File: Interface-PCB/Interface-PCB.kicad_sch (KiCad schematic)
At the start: 16 parts, among them J1 BARREL_JACK_PAD, J2 BARREL_JACK_PAD, J3 GPIO_DEBUG_HEADER, J4 RASPBERRYPI_GPIO_CONN_HEADER, M1 PERISTALTIC_PUMP, M2 PERISTALTIC_PUMP, M3 PERISTALTIC_PUMP, U1 TB6612FNG_BREAKOUT, U2 TB6612FNG_BREAKOUT

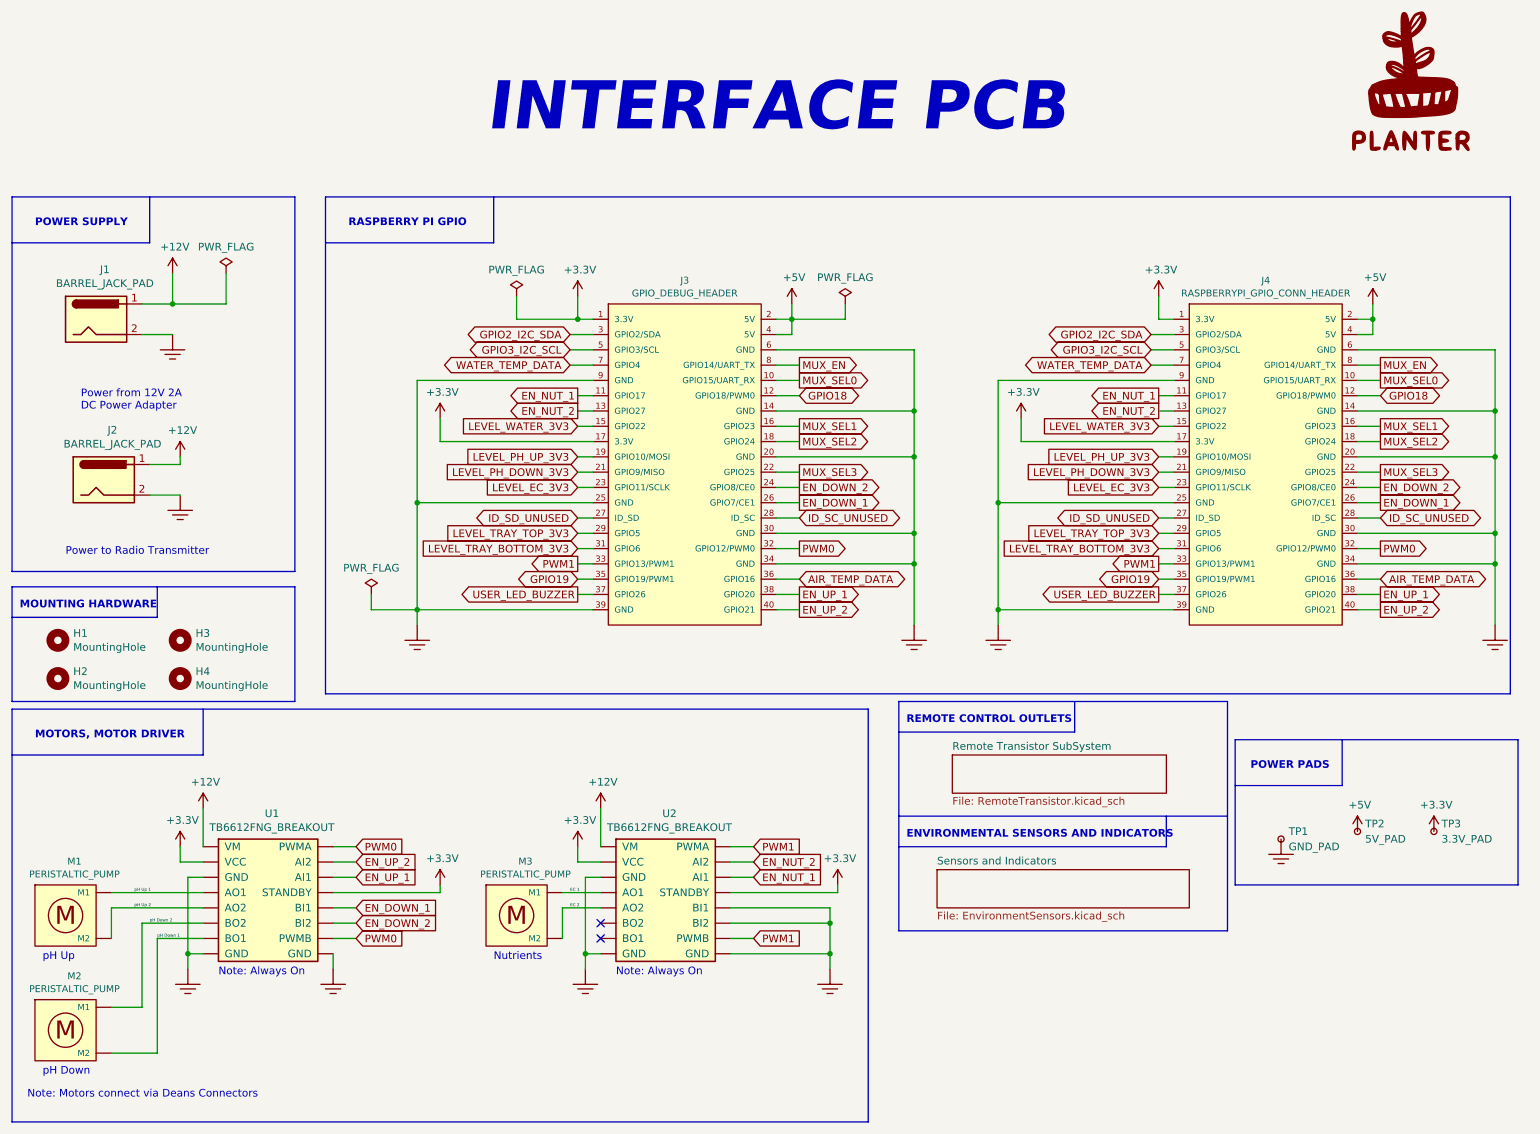
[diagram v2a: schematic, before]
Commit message: Align DIP-socket resistors with 2.54mm pin spacing
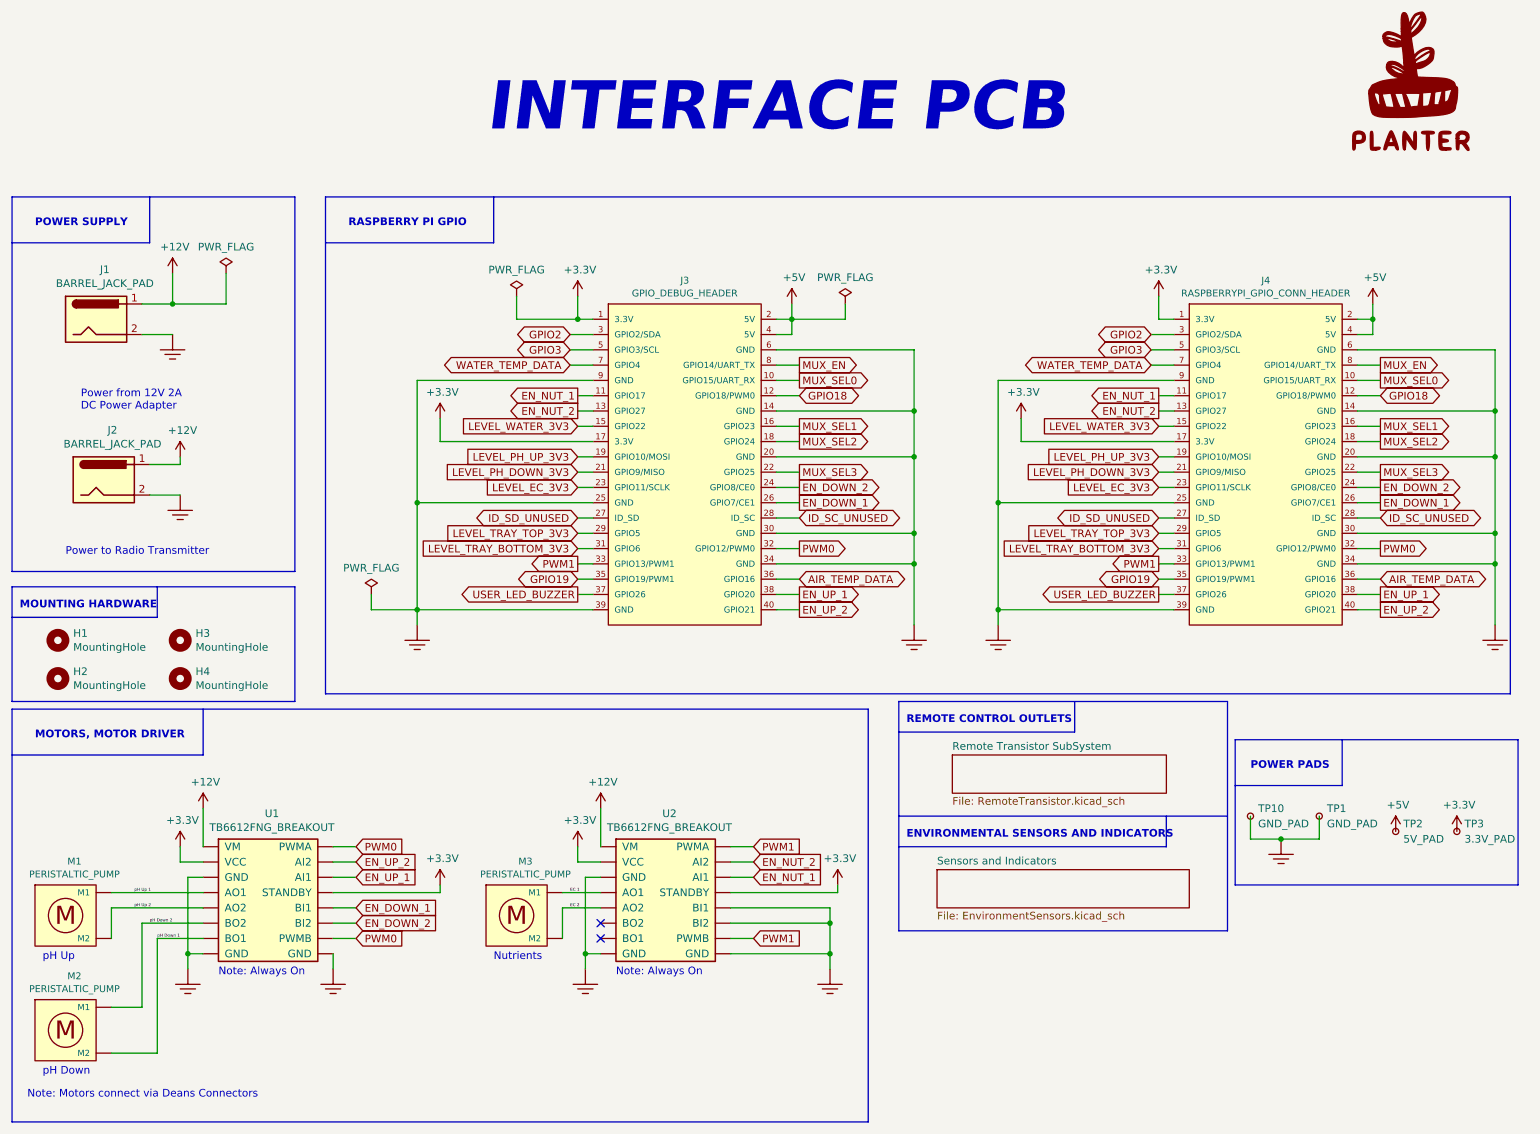
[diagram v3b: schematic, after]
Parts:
- added TP10: GND_PAD, AA_Custom_Components:TestPoint_Pad_5.0x5.0mm, symbol Connector:TestPoint_Small
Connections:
- net GND: now also TP10.1
- net GPIO2_I2C_SDA renamed GPIO2
- net GPIO3_I2C_SCL renamed GPIO3
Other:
- moved on the sheet: TP1, TP2, TP3
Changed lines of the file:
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@@
   (junction (at 151.13 168.91) (diameter 0) (color 0 0 0 0)
+  )
+  (junction (at 226.06 154.94) (diameter 0) (color 0 0 0 0)
   )
   (junction (at 261.62 109.22) (diameter 0) (color 0 0 0 0)
@@
     (stroke (width 0) (type default) (color 0 0 0 0))
   )
+  (wire (pts (xy 232.41 151.13) (xy 232.41 154.94))
+    (stroke (width 0) (type default) (color 0 0 0 0))
+  )
   (polyline (pts (xy 264.16 130.81) (xy 67.31 130.81))
     (stroke (width 0) (type default) (color 0 0 0 0))
@@
     (stroke (width 0) (type default) (color 0 0 0 0))
   )
+  (wire (pts (xy 232.41 154.94) (xy 226.06 154.94))
+    (stroke (width 0) (type default) (color 0 0 0 0))
+  )
   (wire (pts (xy 238.76 96.52) (xy 242.57 96.52))
     (stroke (width 0) (type default) (color 0 0 0 0))
@@
     (stroke (width 0) (type default) (color 0 0 0 0))
   )
+  (wire (pts (xy 220.98 154.94) (xy 226.06 154.94))
+    (stroke (width 0) (type default) (color 0 0 0 0))
+  )
   (wire (pts (xy 72.39 171.45) (xy 68.58 171.45))
     (stroke (width 0) (type default) (color 0 0 0 0))
@@
   )
   (wire (pts (xy 109.22 86.36) (xy 111.76 86.36))
+    (stroke (width 0) (type default) (color 0 0 0 0))
+  )
+  (wire (pts (xy 220.98 151.13) (xy 220.98 154.94))
     (stroke (width 0) (type default) (color 0 0 0 0))
   )
@@
     )
   )
-  (global_label "GPIO3_I2C_SCL" (shape bidirectional) (at 107.95 73.66 180) (fields_autoplaced)
-    (effects (font (size 1.27 1.27)) (justify right))
-    (property "Intersheet References" "${INTERSHEET_REFS}" (id 0) (at 91.4139 73.5806 0)
+  (global_label "GPIO3" (shape bidirectional) (at 107.95 73.66 180) (fields_autoplaced)
+    (effects (font (size 1.27 1.27)) (justify right))
+    (property "Intersheet References" "${INTERSHEET_REFS}" (id 0) (at 99.941 73.5806 0)
       (effects (font (size 1.27 1.27)) (justify right) hide)
     )
@@
     )
   )
-  (global_label "GPIO2_I2C_SDA" (shape bidirectional) (at 107.95 71.12 180) (fields_autoplaced)
-    (effects (font (size 1.27 1.27)) (justify right))
-    (property "Intersheet References" "${INTERSHEET_REFS}" (id 0) (at 91.3534 71.0406 0)
+  (global_label "GPIO2" (shape bidirectional) (at 107.95 71.12 180) (fields_autoplaced)
+    (effects (font (size 1.27 1.27)) (justify right))
+    (property "Intersheet References" "${INTERSHEET_REFS}" (id 0) (at 99.941 71.0406 0)
       (effects (font (size 1.27 1.27)) (justify right) hide)
     )
   )
-  (global_label "GPIO2_I2C_SDA" (shape bidirectional) (at 204.47 71.12 180) (fields_autoplaced)
-    (effects (font (size 1.27 1.27)) (justify right))
-    (property "Intersheet References" "${INTERSHEET_REFS}" (id 0) (at 187.8734 71.0406 0)
+  (global_label "GPIO2" (shape bidirectional) (at 204.47 71.12 180) (fields_autoplaced)
+    (effects (font (size 1.27 1.27)) (justify right))
+    (property "Intersheet References" "${INTERSHEET_REFS}" (id 0) (at 196.461 71.0406 0)
       (effects (font (size 1.27 1.27)) (justify right) hide)
     )
@@
     )
   )
-  (global_label "GPIO3_I2C_SCL" (shape bidirectional) (at 204.47 73.66 180) (fields_autoplaced)
-    (effects (font (size 1.27 1.27)) (justify right))
-    (property "Intersheet References" "${INTERSHEET_REFS}" (id 0) (at 187.9339 73.5806 0)
+  (global_label "GPIO3" (shape bidirectional) (at 204.47 73.66 180) (fields_autoplaced)
+    (effects (font (size 1.27 1.27)) (justify right))
+    (property "Intersheet References" "${INTERSHEET_REFS}" (id 0) (at 196.461 73.5806 0)
       (effects (font (size 1.27 1.27)) (justify right) hide)
     )
@@
     (pin "~")
   )
-  (symbol (lib_id "Connector:TestPoint_Small") (at 251.46 153.67 0) (unit 1)
+  (symbol (lib_id "Connector:TestPoint_Small") (at 255.27 153.67 0) (unit 1)
     (in_bom yes) (on_board yes) (fields_autoplaced)
-    (property "Reference" "TP3" (id 0) (at 252.73 152.3999 0)
+    (property "Reference" "TP3" (id 0) (at 256.54 152.3999 0)
       (effects (font (size 1.27 1.27)) (justify left))
     )
-    (property "Value" "3.3V_PAD" (id 1) (at 252.73 154.9399 0)
+    (property "Value" "3.3V_PAD" (id 1) (at 256.54 154.9399 0)
       (effects (font (size 1.27 1.27)) (justify left))
     )
-    (property "Footprint" "AA_Custom_Components:TestPoint_Pad_5.0x5.0mm" (id 2) (at 256.54 153.67 0)
-      (effects (font (size 1.27 1.27)) hide)
-    )
-    (property "Datasheet" "~" (id 3) (at 256.54 153.67 0)
-      (effects (font (size 1.27 1.27)) hide)
-    )
-    (pin "1")
-  )
-  (symbol (lib_id "Connector:TestPoint_Small") (at 238.76 153.67 0) (unit 1)
+    (property "Footprint" "AA_Custom_Components:TestPoint_Pad_5.0x5.0mm" (id 2) (at 260.35 153.67 0)
+      (effects (font (size 1.27 1.27)) hide)
+    )
+    (property "Datasheet" "~" (id 3) (at 260.35 153.67 0)
+      (effects (font (size 1.27 1.27)) hide)
+    )
+    (pin "1")
+  )
+  (symbol (lib_id "Connector:TestPoint_Small") (at 245.11 153.67 0) (unit 1)
     (in_bom yes) (on_board yes) (fields_autoplaced)
-    (property "Reference" "TP2" (id 0) (at 240.03 152.3999 0)
+    (property "Reference" "TP2" (id 0) (at 246.38 152.3999 0)
       (effects (font (size 1.27 1.27)) (justify left))
     )
-    (property "Value" "5V_PAD" (id 1) (at 240.03 154.9399 0)
+    (property "Value" "5V_PAD" (id 1) (at 246.38 154.9399 0)
       (effects (font (size 1.27 1.27)) (justify left))
     )
-    (property "Footprint" "AA_Custom_Components:TestPoint_Pad_5.0x5.0mm" (id 2) (at 243.84 153.67 0)
-      (effects (font (size 1.27 1.27)) hide)
-    )
-    (property "Datasheet" "~" (id 3) (at 243.84 153.67 0)
-      (effects (font (size 1.27 1.27)) hide)
-    )
-    (pin "1")
-  )
-  (symbol (lib_id "Connector:TestPoint_Small") (at 226.06 154.94 0) (unit 1)
+    (property "Footprint" "AA_Custom_Components:TestPoint_Pad_5.0x5.0mm" (id 2) (at 250.19 153.67 0)
+      (effects (font (size 1.27 1.27)) hide)
+    )
+    (property "Datasheet" "~" (id 3) (at 250.19 153.67 0)
+      (effects (font (size 1.27 1.27)) hide)
+    )
+    (pin "1")
+  )
+  (symbol (lib_id "Connector:TestPoint_Small") (at 232.41 151.13 0) (unit 1)
     (in_bom yes) (on_board yes) (fields_autoplaced)
-    (property "Reference" "TP1" (id 0) (at 227.33 153.6699 0)
+    (property "Reference" "TP1" (id 0) (at 233.68 149.8599 0)
       (effects (font (size 1.27 1.27)) (justify left))
     )
-    (property "Value" "GND_PAD" (id 1) (at 227.33 156.2099 0)
+    (property "Value" "GND_PAD" (id 1) (at 233.68 152.3999 0)
       (effects (font (size 1.27 1.27)) (justify left))
     )
-    (property "Footprint" "AA_Custom_Components:TestPoint_Pad_5.0x5.0mm" (id 2) (at 231.14 154.94 0)
-      (effects (font (size 1.27 1.27)) hide)
-    )
-    (property "Datasheet" "~" (id 3) (at 231.14 154.94 0)
-      (effects (font (size 1.27 1.27)) hide)
-    )
-    (pin "1")
-  )
-  (symbol (lib_id "power:+3.3V") (at 251.46 153.67 0) (unit 1)
-    (in_bom yes) (on_board yes)
-    (property "Reference" "#PWR016" (id 0) (at 251.46 157.48 0)
-      (effects (font (size 1.27 1.27)) hide)
-    )
-    (property "Value" "+3.3V" (id 1) (at 251.841 149.2758 0))
-    (property "Footprint" "" (id 2) (at 251.46 153.67 0)
-      (effects (font (size 1.27 1.27)) hide)
-    )
-    (property "Datasheet" "" (id 3) (at 251.46 153.67 0)
-      (effects (font (size 1.27 1.27)) hide)
-    )
-    (pin "1")
-  )
-  (symbol (lib_id "power:+5V") (at 238.76 153.67 0) (unit 1)
-    (in_bom yes) (on_board yes)
-    (property "Reference" "#PWR014" (id 0) (at 238.76 157.48 0)
-      (effects (font (size 1.27 1.27)) hide)
-    )
-    (property "Value" "+5V" (id 1) (at 239.141 149.2758 0))
-    (property "Footprint" "" (id 2) (at 238.76 153.67 0)
-      (effects (font (size 1.27 1.27)) hide)
-    )
-    (property "Datasheet" "" (id 3) (at 238.76 153.67 0)
+    (property "Footprint" "AA_Custom_Components:TestPoint_Pad_5.0x5.0mm" (id 2) (at 237.49 151.13 0)
+      (effects (font (size 1.27 1.27)) hide)
+    )
+    (property "Datasheet" "~" (id 3) (at 237.49 151.13 0)
+      (effects (font (size 1.27 1.27)) hide)
+    )
+    (pin "1")
+  )
+  (symbol (lib_id "Connector:TestPoint_Small") (at 220.98 151.13 0) (unit 1)
+    (in_bom yes) (on_board yes) (fields_autoplaced)
+    (property "Reference" "TP10" (id 0) (at 222.25 149.8599 0)
+      (effects (font (size 1.27 1.27)) (justify left))
+    )
+    (property "Value" "GND_PAD" (id 1) (at 222.25 152.3999 0)
+      (effects (font (size 1.27 1.27)) (justify left))
+    )
+    (property "Footprint" "AA_Custom_Components:TestPoint_Pad_5.0x5.0mm" (id 2) (at 226.06 151.13 0)
+      (effects (font (size 1.27 1.27)) hide)
+    )
+    (property "Datasheet" "~" (id 3) (at 226.06 151.13 0)
+      (effects (font (size 1.27 1.27)) hide)
+    )
+    (pin "1")
+  )
+  (symbol (lib_id "power:+3.3V") (at 255.27 153.67 0) (unit 1)
+    (in_bom yes) (on_board yes)
+    (property "Reference" "#PWR016" (id 0) (at 255.27 157.48 0)
+      (effects (font (size 1.27 1.27)) hide)
+    )
+    (property "Value" "+3.3V" (id 1) (at 255.651 149.2758 0))
+    (property "Footprint" "" (id 2) (at 255.27 153.67 0)
+      (effects (font (size 1.27 1.27)) hide)
+    )
+    (property "Datasheet" "" (id 3) (at 255.27 153.67 0)
+      (effects (font (size 1.27 1.27)) hide)
+    )
+    (pin "1")
+  )
+  (symbol (lib_id "power:+5V") (at 245.11 153.67 0) (unit 1)
+    (in_bom yes) (on_board yes)
+    (property "Reference" "#PWR014" (id 0) (at 245.11 157.48 0)
+      (effects (font (size 1.27 1.27)) hide)
+    )
+    (property "Value" "+5V" (id 1) (at 245.491 149.2758 0))
+    (property "Footprint" "" (id 2) (at 245.11 153.67 0)
+      (effects (font (size 1.27 1.27)) hide)
+    )
+    (property "Datasheet" "" (id 3) (at 245.11 153.67 0)
       (effects (font (size 1.27 1.27)) hide)
     )
@@
       (reference "TP9") (unit 1) (value "PAD") (footprint "TestPoint:TestPoint_Pad_D1.5mm")
     )
+    (path "/d5bf4c60-be3e-4924-9255-2c110c207ea7"
+      (reference "TP10") (unit 1) (value "GND_PAD") (footprint "AA_Custom_Components:TestPoint_Pad_5.0x5.0mm")
+    )
     (path "/00000000-0000-0000-0000-0000638d4504"
